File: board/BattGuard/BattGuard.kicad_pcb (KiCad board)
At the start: 2 copper layers, 140 x 80 mm, 145 parts, among them J10 Conn_01x01_Pin, J11 Conn_01x01_Pin, J12 Conn_01x01_Pin, J13 Conn_01x01_Pin, J14 Conn_01x01_Pin, J3 Conn_01x22_Pin, J4 Conn_01x22_Pin, J8 GSB4111312HR, J9 Conn_01x01_Pin, Q1 SIR680LDP-T1-RE3, Q7 AO3401A, Q8 2N7002, Q9 AO3401A, U1 BQ25756ERRVR, U2 LMR51420XDDCR, U3 MCP45HV51-ST, U4 INA226, U5 LM317_TO3, U6 TLV76133KVUR, U7 TLV61047DDC

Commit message: 10.19.2026 pcb layout
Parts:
- added C58: 100nF, Capacitor_SMD:C_0805_2012Metric, F.Cu at (204.5, 78.5)
- added C59: 10uF, Capacitor_SMD:C_0805_2012Metric, F.Cu at (207.5, 78.5)
- added J1: OQ0271510000G, BattGuard:AMPHENOL_OQ0271510000G, F.Cu at (110.8, 63.5)
- added Q2: SIR680LDP-T1-RE3, BattGuard:TRANS_SIR680LDP-T1-RE3, F.Cu at (145.5, 65.5)
- added Q3: SIR680LDP-T1-RE3, BattGuard:TRANS_SIR680LDP-T1-RE3, F.Cu at (174.5, 65.5)
- added Q4: SIR680LDP-T1-RE3, BattGuard:TRANS_SIR680LDP-T1-RE3, F.Cu at (174.5, 58.0)
- added R50: 0, Resistor_SMD:R_0805_2012Metric, F.Cu at (157.0, 86.0)
- J3, J4: footprint Connector_PinHeader_2.00mm:PinHeader_1x22_P2.00mm_Vertical -> Connector_PinSocket_2.54mm:PinSocket_1x22_P2.54mm_Vertical
- moved R29 193.7 mm to (246.0, 60.9)
- moved R28 189.1 mm to (241.6, 60.9)
- moved R36 188.9 mm to (246.0, 57.5)
- moved R39 185.4 mm to (241.6, 57.5)
- moved R27 184.5 mm to (237.2, 60.9)
- moved R38 180.7 mm to (237.2, 57.5)
- moved R26 179.9 mm to (232.8, 60.9)
- moved J4 178.8 mm to (255.3, 98.7), turned to -90 degrees
- moved J3 178.8 mm to (255.3, 73.3), turned to -90 degrees
- moved R35 175.5 mm to (232.8, 57.5)
- moved R25 175.3 mm to (228.4, 60.9)
- moved U5 172.2 mm to (227.2, 110.0)
- moved U4 172.1 mm to (195.0, 112.5)
- moved R34 170.9 mm to (228.4, 57.5)
- moved R24 170.8 mm to (224.0, 60.9)
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- renumbered TH1(103AT-2)1 to TH1
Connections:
- C29 pad 2: Net-(C29-Pad2) -> /SW1
- C30 pad 1: Net-(C30-Pad1) -> /SW2
- L1 pad 1: Net-(L1-Pad1) -> /SW1
- L1 pad 2: Net-(U1-SW2) -> /SW2
- Q1 pad 1: Net-(L1-Pad1) -> /SW1
- Q1 pad 2: Net-(U1-SW1) -> /SW1
- Q1 pad 3: Net-(C29-Pad2) -> /SW1
- R12 pad 1: -BATT -> AGND
- R16 pad 2: -BATT -> AGND
- R17 pad 1: +3.3V -> +3V3
- R23 pad 1: +3.3V -> +3V3
- R24 pad 1: +3.3V -> +3V3
- R25 pad 1: +3.3V -> +3V3
- R26 pad 1: +3.3V -> +3V3
- R27 pad 1: +3.3V -> +3V3
- R28 pad 1: +3.3V -> +3V3
- R29 pad 1: +3.3V -> +3V3
- R32 pad 1: Net-(U7-SW) -> /+18.5V
- R7 pad 2: -BATT -> AGND
- TH1 pad 2: -BATT -> AGND
- U1 pad 10: -BATT -> AGND
- U1 pad 18: Net-(U1-SW2) -> /SW2
- U1 pad 28: Net-(U1-SW1) -> /SW1
- U1 pad 9: -BATT -> AGND
- U3 pad 1: +3.3V -> +3V3
- U3 pad 8: +3.3V -> +3V3
- U4 pad 6: +3.3V -> +3V3
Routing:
- added copper zone on In2.Cu, net +3V3
- added copper zone on In2.Cu, net +5V
- added copper zone on B.Cu, net -BATT
- added copper zone on In1.Cu, net -BATT
- added copper zone on In2.Cu, net -BATT
- added copper zone on In2.Cu, net /+18.5V
- added copper zone on In2.Cu, net /Vsys
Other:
- board size 140 x 80 mm -> 160 x 80 mm
- copper layers 2 -> 4

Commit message: 10.19.2026 pcb v1 no route
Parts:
- added J15: Conn_01x01_Pin, MountingHole:MountingHole_2.2mm_M2_DIN965_Pad, F.Cu at (111.7, 101.2)
- added J17: S5B-XH-A, TeamLib:JST_S5B-XH-A, F.Cu at (165.6, 134.3)
- added J2: Barrel_Jack, Connector_BarrelJack:BarrelJack_CUI_PJ-063AH_Horizontal_CircularHoles, F.Cu at (121.7, 62.0)
- added J5: Conn_01x02_Pin(xt60), Connector_AMASS:AMASS_XT60IPW-M_1x03_P7.20mm_Horizontal, F.Cu at (186.1, 121.8)
- added J7: EC5 JUMP CONNECTOR, Connector_AMASS:AMASS_XT60PW-M_1x02_P7.20mm_Horizontal, F.Cu at (203.6, 122.0)
- J1: footprint BattGuard:AMPHENOL_OQ0271510000G -> BattGuard:CONN_SD-39522-003_02P_MOL
- moved D5 52.1 mm to (155.9, 119.6), turned to 90 degrees
- moved R21 32.4 mm to (211.8, 92.0)
- moved R20 31.4 mm to (207.4, 92.0)
- moved R19 28.5 mm to (203.0, 92.0)
- moved R1 23.5 mm to (103.5, 82.5), turned to 0 degrees
- moved C2 17.6 mm to (107.9, 82.5), turned to 0 degrees
- moved D1 13.9 mm to (121.8, 76.9)
- moved C1 12.0 mm to (112.3, 82.5), turned to 0 degrees
- moved C3 4.51 mm to (116.7, 82.5), turned to 0 degrees
- moved R18 3.24 mm to (200.0, 116.3)
- moved D2 2.51 mm to (121.8, 69.0)
- turned C10 to -90 degrees
- turned C12 to -90 degrees
- turned C14 to -90 degrees
- turned C21 to -90 degrees
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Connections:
- D1 pad 1: (no net) -> VCC
- D1 pad 2: (no net) -> Net-(D1-Pad2)
- D2 pad 1: (no net) -> VCC
- D2 pad 2: (no net) -> Net-(D2-Pad2)
- D5 pad 1: (no net) -> /+18.5V
- D5 pad 2: (no net) -> Net-(U7-SW)
- J1 pad 2: Net-(D1-PadA) -> Net-(D1-Pad2)
- J3 pad 8: /GPI15 -> /GPIO15
- J3 pad 9: /GPI16 -> /GPIO16
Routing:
- net /Vsystem: vias 0 -> 15
- net /Vsys: vias 0 -> 29
- net /Vout: vias 0 -> 29
- net -BATT: vias 0 -> 78
- added copper zone on F.Cu, net +BATT
- added copper zone on F.Cu, net -BATT
- added copper zone on F.Cu, net /SW1
- added copper zone on F.Cu, net /SW2
- added copper zone on B.Cu, net /Vout
- added copper zone on F.Cu, net /Vout
- added copper zone on B.Cu, net /Vsys
- added copper zone on F.Cu, net /Vsys
- added copper zone on B.Cu, net /Vsystem
- added copper zone on F.Cu, net /Vsystem
- added copper zone on F.Cu, net Net-(D1-Pad2)
- added copper zone on F.Cu, net Net-(D2-Pad2)
- added copper zone on F.Cu, net VCC

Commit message: 10.19.2026 v2
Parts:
- removed Q9: AO3401A, Package_TO_SOT_SMD:SOT-23
- removed R20: 100k, Resistor_SMD:R_0805_2012Metric
- D10, D11, D7, D8, D9: footprint TestPoint:TestPoint_Pad_1.0x1.0mm -> LED_THT:LED_D1.8mm_W1.8mm_H2.4mm_Horizontal_O1.27mm_Z4.9mm
- R19: value 100 -> 1k
- R21: value 100k -> 1K
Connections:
- C1 pad 1: -BATT -> GND
- C10 pad 2: -BATT -> GND
- C11 pad 2: -BATT -> GND
- C12 pad 2: -BATT -> GND
- C13 pad 2: -BATT -> GND
- C14 pad 2: -BATT -> GND
- C16 pad 2: -BATT -> GND
- C17 pad 1: -BATT -> GND
- C18 pad 2: -BATT -> GND
- C19 pad 2: -BATT -> GND
- C2 pad 2: -BATT -> GND
- C20 pad 2: -BATT -> GND
- C21 pad 2: -BATT -> GND
- C22 pad 2: -BATT -> GND
- C23 pad 2: -BATT -> GND
- C24 pad 2: -BATT -> GND
- C25 pad 2: -BATT -> GND
- C26 pad 2: -BATT -> GND
- C27 pad 2: -BATT -> GND
- C28 pad 2: -BATT -> GND
- C3 pad 2: -BATT -> GND
- C32 pad 1: -BATT -> GND
- C33 pad 2: -BATT -> GND
- C34 pad 2: -BATT -> GND
- C35 pad 2: -BATT -> GND
- C36 pad 2: -BATT -> GND
- C37 pad 2: -BATT -> GND
- C38 pad 2: -BATT -> GND
- C39 pad 2: -BATT -> GND
- C4 pad 2: -BATT -> GND
- C40 pad 2: -BATT -> GND
- C41 pad 2: -BATT -> GND
- C42 pad 1: Net-(Q9-D) -> Net-(Q7-D)
- C42 pad 2: -BATT -> GND
- C44 pad 2: -BATT -> GND
- C45 pad 2: -BATT -> GND
- C46 pad 2: -BATT -> GND
- C47 pad 2: -BATT -> GND
- C48 pad 2: -BATT -> GND
- C49 pad 2: -BATT -> GND
- C5 pad 2: -BATT -> GND
- C50 pad 2: -BATT -> GND
- C51 pad 2: -BATT -> GND
- C52 pad 2: -BATT -> GND
- C53 pad 2: -BATT -> GND
- C54 pad 2: -BATT -> GND
- C56 pad 2: -BATT -> GND
- C57 pad 2: -BATT -> GND
- C58 pad 2: -BATT -> GND
- C59 pad 2: -BATT -> GND
- C6 pad 2: -BATT -> GND
- C7 pad 2: -BATT -> GND
- C8 pad 2: -BATT -> GND
- C9 pad 2: -BATT -> GND
- D10 pad 1: -BATT -> GND
- D11 pad 1: -BATT -> GND
- D6 pad 1: -BATT -> GND
- D7 pad 1: -BATT -> GND
- D8 pad 1: -BATT -> GND
- D9 pad 1: -BATT -> GND
- J1 pad 1: -BATT -> GND
- J17 pad 1: -BATT -> GND
- J2 pad 2: -BATT -> GND
- J3 pad 22: -BATT -> GND
- J4 pad 1: -BATT -> GND
- J4 pad 21: -BATT -> GND
- J4 pad 22: -BATT -> GND
- J5 pad 2: -BATT -> GND
- J7 pad 2: -BATT -> GND
- J8 pad 4: -BATT -> GND
- J8 pad 7: -BATT -> GND
- Q2 pad 1: -BATT -> GND
- Q2 pad 2: -BATT -> GND
- Q2 pad 3: -BATT -> GND
- Q3 pad 1: -BATT -> GND
- Q3 pad 2: -BATT -> GND
- Q3 pad 3: -BATT -> GND
- Q8 pad 1: Net-(Q8-G) -> /GPIO4
- Q8 pad 2: -BATT -> GND
- R18 pad 1: Net-(Q7-D) -> Net-(Q7-S)
- R19 pad 1: /GPIO4 -> GND
- R19 pad 2: Net-(Q8-G) -> /GPIO4
- R22 pad 1: Net-(Q9-D) -> Net-(Q7-D)
- R31 pad 1: -BATT -> GND
- R33 pad 2: -BATT -> GND
- R50 pad 2: -BATT -> GND
- U1 pad 17: -BATT -> GND
- U1 pad 22: -BATT -> GND
- U1 pad 37: -BATT -> GND
- U2 pad 1: -BATT -> GND
- U3 pad 10: -BATT -> GND
- U3 pad 11: -BATT -> GND
- U3 pad 3: -BATT -> GND
- U3 pad 5: -BATT -> GND
- U3 pad 6: -BATT -> GND
- U3 pad 9: -BATT -> GND
- U4 pad 1: -BATT -> GND
- U4 pad 10: Net-(Q9-D) -> Net-(Q7-D)
- U4 pad 2: -BATT -> GND
- U4 pad 7: -BATT -> GND
- U5 pad 3: Net-(Q7-D) -> Net-(Q7-S)
- U6 pad 1: -BATT -> GND
- U7 pad 2: -BATT -> GND
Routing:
- net /GPIO2: track 0.00 -> 144.1 mm, vias 0 -> 2
- net /GPIO42: track 0.00 -> 121.5 mm, vias 0 -> 3
- net /GPIO1: track 0.00 -> 109.4 mm, vias 0 -> 2
- net /GPIO41: track 0.00 -> 97.2 mm, vias 0 -> 3
- net +5V: track 0.00 -> 93.2 mm, vias 0 -> 8
- net /GPIO10: track 0.00 -> 82.9 mm, vias 0 -> 3
- net /GPIO4: track 0.00 -> 81.2 mm, vias 0 -> 2
- net Net-(Q7-S): track 0.00 -> 78.2 mm
- net Net-(U1-DRV_SUP): track 0.00 -> 77.6 mm, vias 0 -> 3
- net /GPIO16: track 0.00 -> 68.8 mm, vias 0 -> 2
- net /GPIO39: track 0.00 -> 66.3 mm, vias 0 -> 1
- net /GPIO40: track 0.00 -> 58.8 mm, vias 0 -> 1
- net /GPIO21: track 0.00 -> 53.6 mm, vias 0 -> 3
- net /GPIO47: track 0.00 -> 48.0 mm, vias 0 -> 2
- net Net-(J8-VBUS): track 0.00 -> 47.5 mm
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- added copper zone on B.Cu, net GND
- added copper zone on F.Cu, net GND
- added copper zone on In1.Cu, net GND
- added copper zone on In2.Cu, net GND
- removed copper zone on B.Cu, net -BATT
- removed copper zone on F.Cu, net -BATT
- removed copper zone on In1.Cu, net -BATT
- removed copper zone on In2.Cu, net -BATT

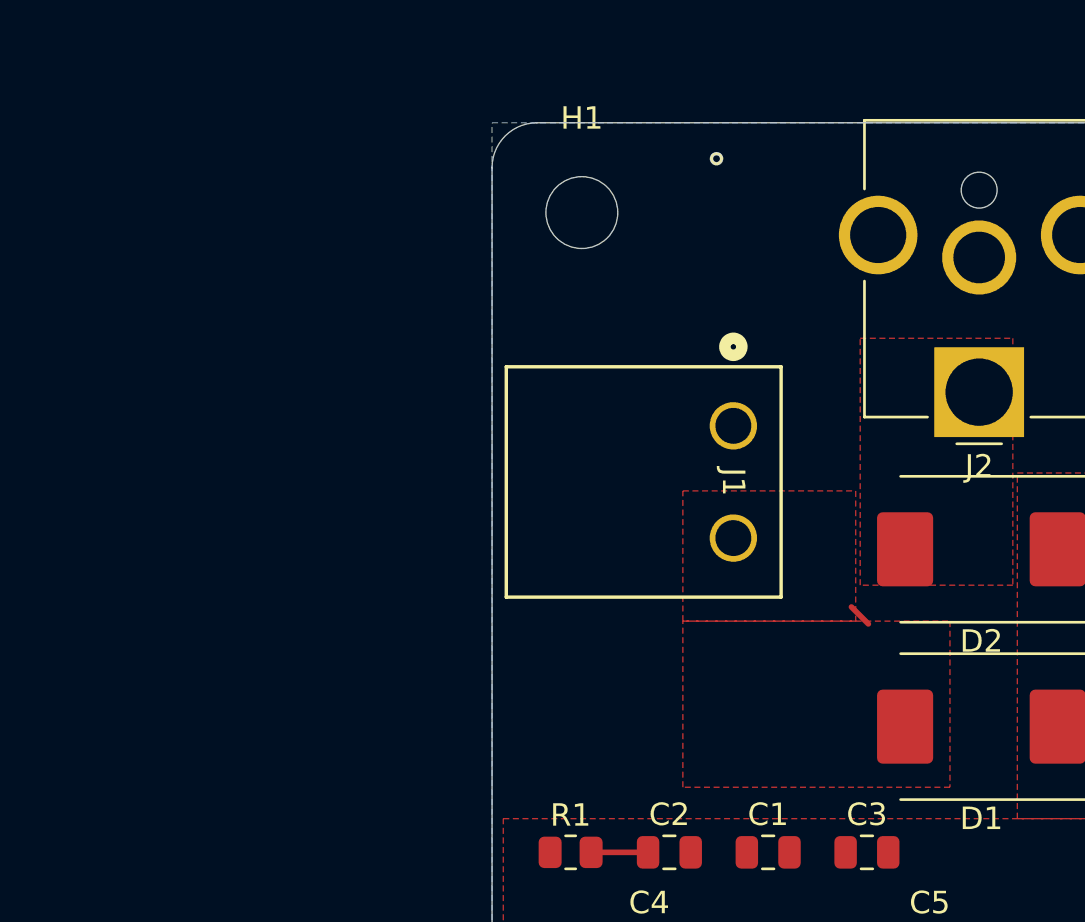
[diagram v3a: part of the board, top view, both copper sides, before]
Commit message: Updated ESP32 Devkit, Added Input protection
Reverse polarity BQ Input protection, labeled input blocks, added model for U2
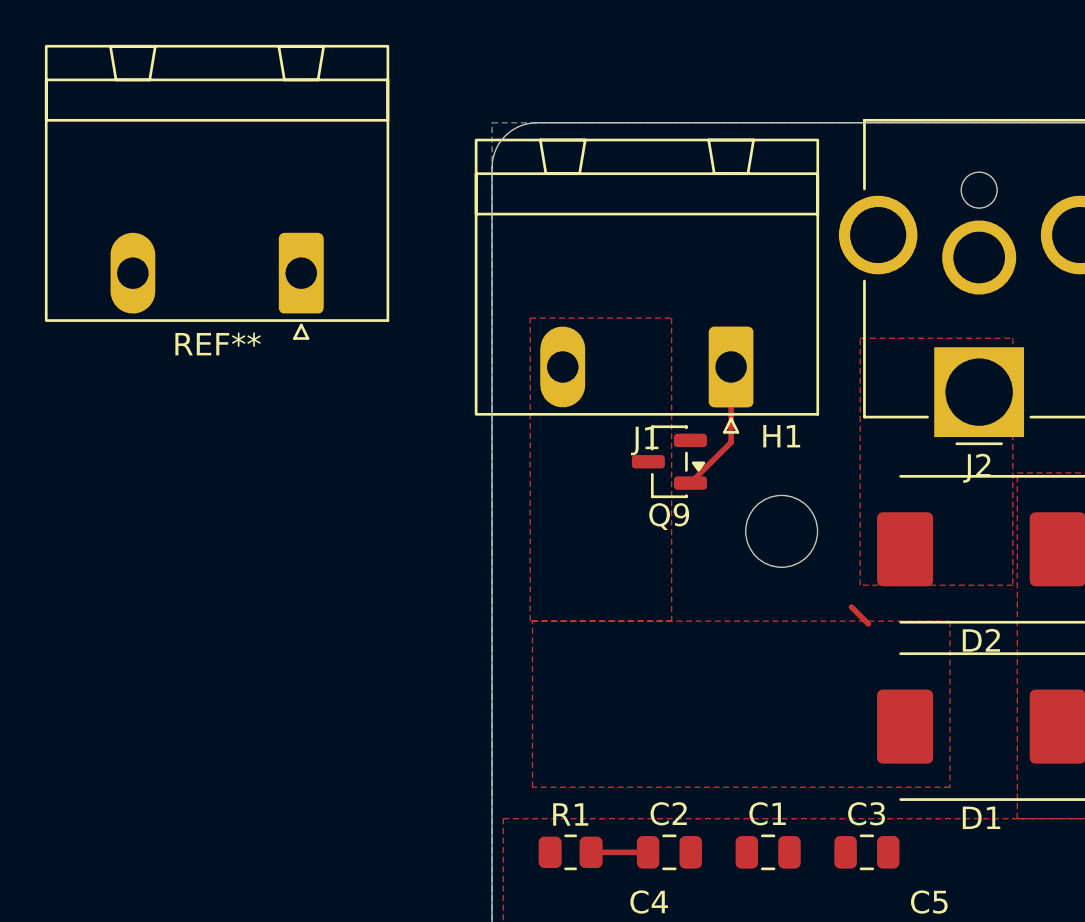
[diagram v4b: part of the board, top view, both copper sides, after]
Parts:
- added Q9: AO3401A, Package_TO_SOT_SMD:SOT-23, F.Cu at (107.9, 65.1)
- added REF**: PhoenixContact_GMSTBA_2,5_2-G_1x02_P7.50mm_Horizontal, Connector_Phoenix_GMSTB:PhoenixContact_GMSTBA_2,5_2-G_1x02_P7.50mm_Horizontal, F.Cu at (91.5, 56.7)
- J1: footprint BattGuard:CONN_SD-39522-003_02P_MOL -> Connector_Phoenix_GMSTB:PhoenixContact_GMSTBA_2,5_2-G_1x02_P7.50mm_Horizontal
- moved H1 16.8 mm to (112.9, 68.2)
- moved J1 2.62 mm to (110.7, 60.9), turned to 180 degrees
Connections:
- D1 pad 2: Net-(D1-Pad2) -> Net-(Q9-S)
- J1 pad 2: Net-(D1-Pad2) -> (no net)
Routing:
- net GND: track 0.00 -> 5.92 mm, vias 77 -> 76
- added copper zone on F.Cu, net Net-(Q9-D)
- added copper zone on F.Cu, net Net-(Q9-S)
- removed copper zone on F.Cu, net Net-(D1-Pad2)

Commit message: 10.20.2026 Changes
Fixed connectors, pours, some NCs
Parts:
- removed REF**: PhoenixContact_GMSTBA_2,5_2-G_1x02_P7.50mm_Horizontal, Connector_Phoenix_GMSTB:PhoenixContact_GMSTBA_2,5_2-G_1x02_P7.50mm_Horizontal
- R22: value .1 -> 0.05
- moved Q9 7.23 mm to (106.0, 72.1), turned to 90 degrees
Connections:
- C1 pad 2: VCC -> VAC
- C3 pad 1: VCC -> VAC
- C4 pad 1: VCC -> VAC
- C5 pad 1: VCC -> VAC
- D1 pad 1: VCC -> VAC
- D2 pad 1: VCC -> VAC
- J1 pad 2: (no net) -> VCC
- Q9 pad 3: Net-(Q9-D) -> VCC
- R1 pad 1: VCC -> VAC
- R2 pad 1: VCC -> VAC
- R3 pad 1: VCC -> VAC
- R5 pad 1: VCC -> VAC
- U1 pad 32: VCC -> VAC
- U1 pad 33: VCC -> VAC
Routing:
- net Net-(Q9-S): track 0.00 -> 13.1 mm
- net /Vsystem: track 0.00 -> 9.79 mm
- net GND: track 5.92 -> 3.82 mm, vias 76 -> 78
- net /TS: track 38.5 -> 40.6 mm, vias 2 -> 3
- net Net-(D1-Pad2): track 1.07 -> 0.00 mm
- removed copper zone on F.Cu, net Net-(Q9-D)

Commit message: 10.28.2026 push
test push working on rn
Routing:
- net /Vsys: track 6.24 -> 7.35 mm
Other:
- board text added: "BattGuard_V1"
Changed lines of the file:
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@@
 		(layer "Edge.Cuts")
+	)
+	(gr_text "BattGuard_V1"
+		(at 251.5 69.5 90)
+		(layer "F.SilkS")
+		(effects
+			(font
+				(size 1.5 1.5)
+				(thickness 0.3)
+				(bold yes)
+			)
+			(justify left bottom)
+		)
 	)
 	(segment
@@
 	)
 	(segment
-		(start 144.201 81.3823)
-		(end 144.201 81.801)
+		(start 149.9375 82)
+		(end 145.4125 82)
 		(width 1.0268)
 		(layer "F.Cu")
@@
 	)
 	(segment
-		(start 144.201 81.801)
-		(end 144.4 82)
-		(width 3)
-		(layer "F.Cu")
-		(net "/Vsys")
-	)
-	(segment
-		(start 144.4 82)
-		(end 149.9375 82)
+		(start 145.4125 82)
+		(end 143.4125 80)
 		(width 1.0268)
 		(layer "F.Cu")
